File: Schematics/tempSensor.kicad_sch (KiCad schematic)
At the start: 0 parts

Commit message: Temp Sensors Circuitry
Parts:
- added A? (x4): ZTP-148SRC1, XDCR_ZTP-148SRC1, symbol SFRLibraries:ZTP-148SRC1
- added D?: D_Schottky, symbol Device:D_Schottky
- added R? (x4): 100k, symbol Device:R_Small_US
- added R? (x8): 1k, symbol Device:R_Small_US
- added R?: 10k, symbol Device:R_Small_US
- added U? (x2): AD8539ARMZ-REEL, RM_8_ADI, symbol SFRLibraries:AD8539ARMZ-REEL
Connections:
- new net: A?.2 (THERMOPILE), U?.3 (INA+) (x2)
- new net: R?.1, U?.2 (INA-) (x2)
- new net: A?.2 (THERMOPILE), U?.5 (INB+) (x2)
- new net: R?.1, U?.6 (INB-) (x2)
- new net Earth: A?.1 (THERMISTOR_GND), A?.1 (THERMISTOR_GND), A?.1 (THERMISTOR_GND), A?.1 (THERMISTOR_GND), D?.2 (A), U?.4 (V-), U?.4 (V-)
- new net Shifted Ground: A?.4 (THERMOPILE_GND), A?.4 (THERMOPILE_GND), A?.4 (THERMOPILE_GND), A?.4 (THERMOPILE_GND), D?.1 (K), R?.2, R?.2, R?.2, R?.2, R?.2
- new net ThermistorA: A?.3 (THERMISTOR), R?.2
- new net ThermistorB: A?.3 (THERMISTOR), R?.2
- new net ThermistorC: A?.3 (THERMISTOR), R?.2
- new net ThermistorD: A?.3 (THERMISTOR), R?.2
- new net ThermopileA: R?.1, R?.2, U?.7 (OUTB)
- new net ThermopileB: R?.1, R?.2, U?.1 (OUTA)
- new net ThermopileC: R?.1, R?.2, U?.7 (OUTB)
- new net ThermopileD: R?.1, R?.2, U?.1 (OUTA)
- new net VCC: R?.1, R?.1, R?.1, R?.1, R?.1, U?.8 (V+), U?.8 (V+)
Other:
- note added: "Create virtual ground for op amps so if thermopile goes negative relative to ground it will still be amplified as a positive voltage"
- note added: "Non-Inverting Op Amp"
- note added: "Voltage Divider for Thermistor"

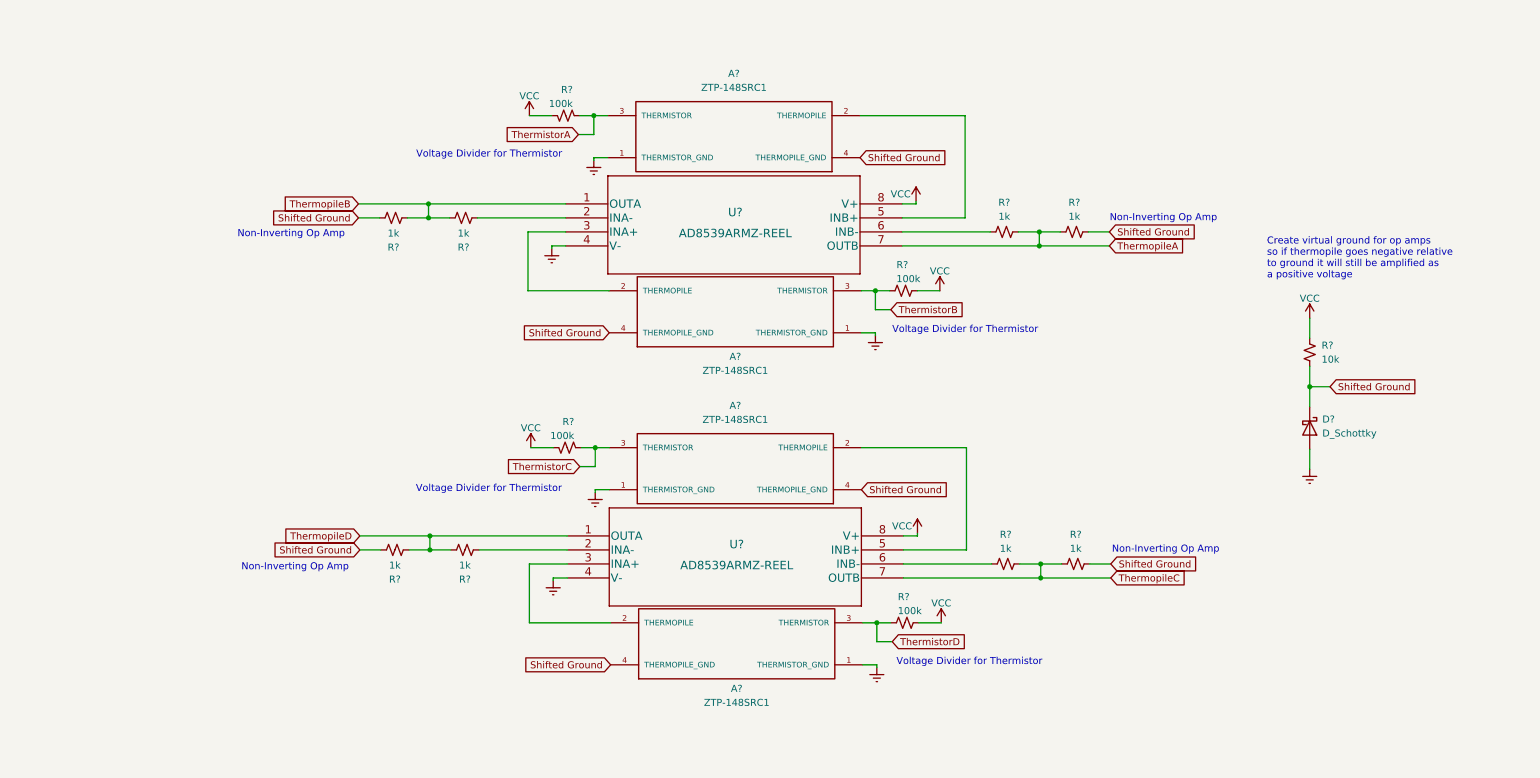
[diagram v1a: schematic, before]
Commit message: Changed MCU
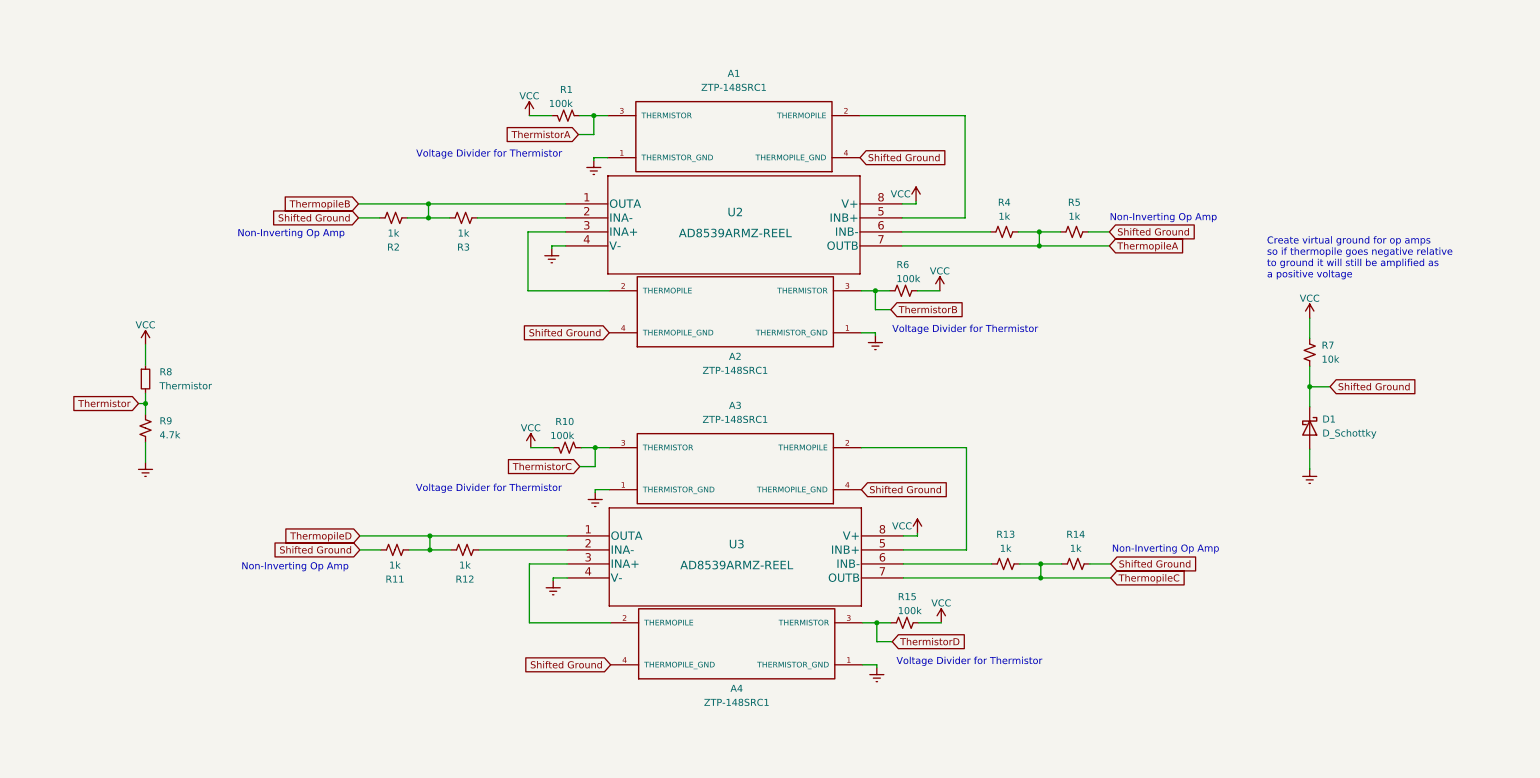
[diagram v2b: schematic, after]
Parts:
- added R8: Thermistor, symbol Device:R_Small
- added R9: 4.7k, symbol Device:R_Small_US
- gave numbers to parts that had none: 20
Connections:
- net Earth: now also R9.2
- net VCC: now also R8.1
- new net Thermistor: R8.2, R9.1

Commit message: Added Footprints
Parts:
- A1, A2, A3, A4: footprint XDCR_ZTP-148SRC1 -> SFRFootprints:Thermopile
- D1: footprint (none) -> Diode_SMD:D_SOD-323
- R1, R10, R11, R12, R13, R14, R15, R2, R3, R4, R5, R6, R7, R9: footprint (none) -> Resistor_SMD:R_0603_1608Metric_Pad0.98x0.95mm_HandSolder
- R8: footprint (none) -> Resistor_SMD:R_1206_3216Metric_Pad1.30x1.75mm_HandSolder
- U2, U3: footprint RM_8_ADI -> SFRFootprints:AD8539ARMZ-REEL
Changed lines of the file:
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@@
       (effects (font (size 1.27 1.27)) (justify left))
     )
-    (property "Footprint" "" (id 2) (at 40.64 107.95 0)
+    (property "Footprint" "Resistor_SMD:R_0603_1608Metric_Pad0.98x0.95mm_HandSolder" (id 2) (at 40.64 107.95 0)
       (effects (font (size 1.27 1.27)) hide)
     )
@@
     (property "Reference" "A4" (id 0) (at 147.828 155.194 0))
     (property "Value" "ZTP-148SRC1" (id 1) (at 147.828 157.734 0))
-    (property "Footprint" "XDCR_ZTP-148SRC1" (id 2) (at 137.668 131.191 0)
+    (property "Footprint" "SFRFootprints:Thermopile" (id 2) (at 137.668 131.191 0)
       (effects (font (size 1.27 1.27)) (justify left bottom) hide)
     )
@@
       (effects (font (size 1.27 1.27)) (justify left))
     )
-    (property "Footprint" "" (id 2) (at 116.84 51.308 0)
+    (property "Footprint" "Resistor_SMD:R_0603_1608Metric_Pad0.98x0.95mm_HandSolder" (id 2) (at 116.84 51.308 0)
       (effects (font (size 1.27 1.27)) hide)
     )
@@
       (effects (font (size 1.524 1.524)))
     )
-    (property "Footprint" "RM_8_ADI" (id 2) (at 147.32 61.214 0)
+    (property "Footprint" "SFRFootprints:AD8539ARMZ-REEL" (id 2) (at 147.32 61.214 0)
       (effects (font (size 1.524 1.524)) hide)
     )
@@
       (effects (font (size 1.27 1.27)) (justify left))
     )
-    (property "Footprint" "" (id 2) (at 117.094 111.506 0)
+    (property "Footprint" "Resistor_SMD:R_0603_1608Metric_Pad0.98x0.95mm_HandSolder" (id 2) (at 117.094 111.506 0)
       (effects (font (size 1.27 1.27)) hide)
     )
@@
     (property "Reference" "R2" (id 0) (at 85.598 75.184 90))
     (property "Value" "1k" (id 1) (at 85.598 72.644 90))
-    (property "Footprint" "" (id 2) (at 85.598 69.85 0)
+    (property "Footprint" "Resistor_SMD:R_0603_1608Metric_Pad0.98x0.95mm_HandSolder" (id 2) (at 85.598 69.85 0)
       (effects (font (size 1.27 1.27)) hide)
     )
@@
     (property "Reference" "R13" (id 0) (at 196.596 127.254 90))
     (property "Value" "1k" (id 1) (at 196.596 129.794 90))
-    (property "Footprint" "" (id 2) (at 196.596 132.588 0)
+    (property "Footprint" "Resistor_SMD:R_0603_1608Metric_Pad0.98x0.95mm_HandSolder" (id 2) (at 196.596 132.588 0)
       (effects (font (size 1.27 1.27)) hide)
     )
@@
       (effects (font (size 1.524 1.524)))
     )
-    (property "Footprint" "RM_8_ADI" (id 2) (at 147.574 121.412 0)
+    (property "Footprint" "SFRFootprints:AD8539ARMZ-REEL" (id 2) (at 147.574 121.412 0)
       (effects (font (size 1.524 1.524)) hide)
     )
@@
     (property "Reference" "R4" (id 0) (at 196.342 67.056 90))
     (property "Value" "1k" (id 1) (at 196.342 69.596 90))
-    (property "Footprint" "" (id 2) (at 196.342 72.39 0)
+    (property "Footprint" "Resistor_SMD:R_0603_1608Metric_Pad0.98x0.95mm_HandSolder" (id 2) (at 196.342 72.39 0)
       (effects (font (size 1.27 1.27)) hide)
     )
@@
     (property "Reference" "R5" (id 0) (at 209.042 67.056 90))
     (property "Value" "1k" (id 1) (at 209.042 69.596 90))
-    (property "Footprint" "" (id 2) (at 209.042 72.39 0)
+    (property "Footprint" "Resistor_SMD:R_0603_1608Metric_Pad0.98x0.95mm_HandSolder" (id 2) (at 209.042 72.39 0)
       (effects (font (size 1.27 1.27)) hide)
     )
@@
     (property "Reference" "R11" (id 0) (at 85.852 135.382 90))
     (property "Value" "1k" (id 1) (at 85.852 132.842 90))
-    (property "Footprint" "" (id 2) (at 85.852 130.048 0)
+    (property "Footprint" "Resistor_SMD:R_0603_1608Metric_Pad0.98x0.95mm_HandSolder" (id 2) (at 85.852 130.048 0)
       (effects (font (size 1.27 1.27)) hide)
     )
@@
       (effects (font (size 1.27 1.27)) (justify left))
     )
-    (property "Footprint" "" (id 2) (at 251.714 94.234 0)
+    (property "Footprint" "Resistor_SMD:R_0603_1608Metric_Pad0.98x0.95mm_HandSolder" (id 2) (at 251.714 94.234 0)
       (effects (font (size 1.27 1.27)) hide)
     )
@@
       (effects (font (size 1.27 1.27)) (justify left))
     )
-    (property "Footprint" "" (id 2) (at 178.308 143.256 0)
+    (property "Footprint" "Resistor_SMD:R_0603_1608Metric_Pad0.98x0.95mm_HandSolder" (id 2) (at 178.308 143.256 0)
       (effects (font (size 1.27 1.27)) hide)
     )
@@
     (property "Reference" "A3" (id 0) (at 147.574 103.886 0))
     (property "Value" "ZTP-148SRC1" (id 1) (at 147.574 106.426 0))
-    (property "Footprint" "XDCR_ZTP-148SRC1" (id 2) (at 157.734 99.441 0)
+    (property "Footprint" "SFRFootprints:Thermopile" (id 2) (at 157.734 99.441 0)
       (effects (font (size 1.27 1.27)) (justify left bottom) hide)
     )
@@
       (effects (font (size 1.27 1.27)) (justify left))
     )
-    (property "Footprint" "" (id 2) (at 40.64 99.06 0)
+    (property "Footprint" "Resistor_SMD:R_1206_3216Metric_Pad1.30x1.75mm_HandSolder" (id 2) (at 40.64 99.06 0)
       (effects (font (size 1.27 1.27)) hide)
     )
@@
     (property "Reference" "R12" (id 0) (at 98.552 135.382 90))
     (property "Value" "1k" (id 1) (at 98.552 132.842 90))
-    (property "Footprint" "" (id 2) (at 98.552 130.048 0)
+    (property "Footprint" "Resistor_SMD:R_0603_1608Metric_Pad0.98x0.95mm_HandSolder" (id 2) (at 98.552 130.048 0)
       (effects (font (size 1.27 1.27)) hide)
     )
@@
     (property "Reference" "R14" (id 0) (at 209.296 127.254 90))
     (property "Value" "1k" (id 1) (at 209.296 129.794 90))
-    (property "Footprint" "" (id 2) (at 209.296 132.588 0)
+    (property "Footprint" "Resistor_SMD:R_0603_1608Metric_Pad0.98x0.95mm_HandSolder" (id 2) (at 209.296 132.588 0)
       (effects (font (size 1.27 1.27)) hide)
     )
@@
     (property "Reference" "A1" (id 0) (at 147.32 43.688 0))
     (property "Value" "ZTP-148SRC1" (id 1) (at 147.32 46.228 0))
-    (property "Footprint" "XDCR_ZTP-148SRC1" (id 2) (at 157.48 39.243 0)
+    (property "Footprint" "SFRFootprints:Thermopile" (id 2) (at 157.48 39.243 0)
       (effects (font (size 1.27 1.27)) (justify left bottom) hide)
     )
@@
     (property "Reference" "R3" (id 0) (at 98.298 75.184 90))
     (property "Value" "1k" (id 1) (at 98.298 72.644 90))
-    (property "Footprint" "" (id 2) (at 98.298 69.85 0)
+    (property "Footprint" "Resistor_SMD:R_0603_1608Metric_Pad0.98x0.95mm_HandSolder" (id 2) (at 98.298 69.85 0)
       (effects (font (size 1.27 1.27)) hide)
     )
@@
     (property "Reference" "A2" (id 0) (at 147.574 94.996 0))
     (property "Value" "ZTP-148SRC1" (id 1) (at 147.574 97.536 0))
-    (property "Footprint" "XDCR_ZTP-148SRC1" (id 2) (at 137.414 70.993 0)
+    (property "Footprint" "SFRFootprints:Thermopile" (id 2) (at 137.414 70.993 0)
       (effects (font (size 1.27 1.27)) (justify left bottom) hide)
     )
@@
       (effects (font (size 1.27 1.27)) (justify left))
     )
-    (property "Footprint" "" (id 2) (at 178.054 83.058 0)
+    (property "Footprint" "Resistor_SMD:R_0603_1608Metric_Pad0.98x0.95mm_HandSolder" (id 2) (at 178.054 83.058 0)
       (effects (font (size 1.27 1.27)) hide)
     )
@@
       (effects (font (size 1.27 1.27)) (justify left))
     )
-    (property "Footprint" "" (id 2) (at 251.714 107.95 0)
-      (effects (font (size 1.27 1.27)) hide)
-    )
+    (property "Footprint" "Diode_SMD:D_SOD-323" (id 2) (at 251.714 107.95 0)
+      (effects (font (size 1.27 1.27)) hide)
+    )

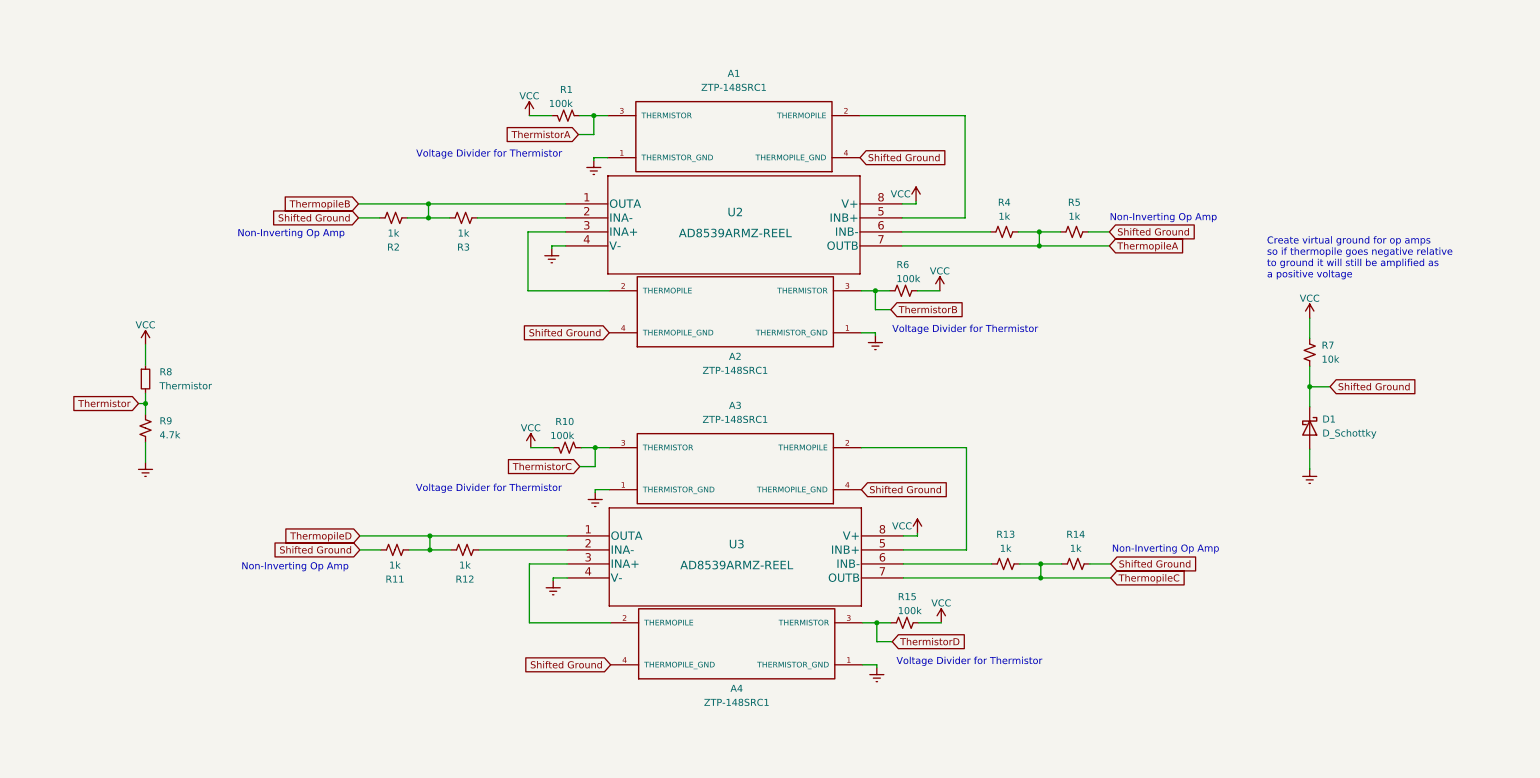
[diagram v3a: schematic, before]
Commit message: Fixed IR Sensor
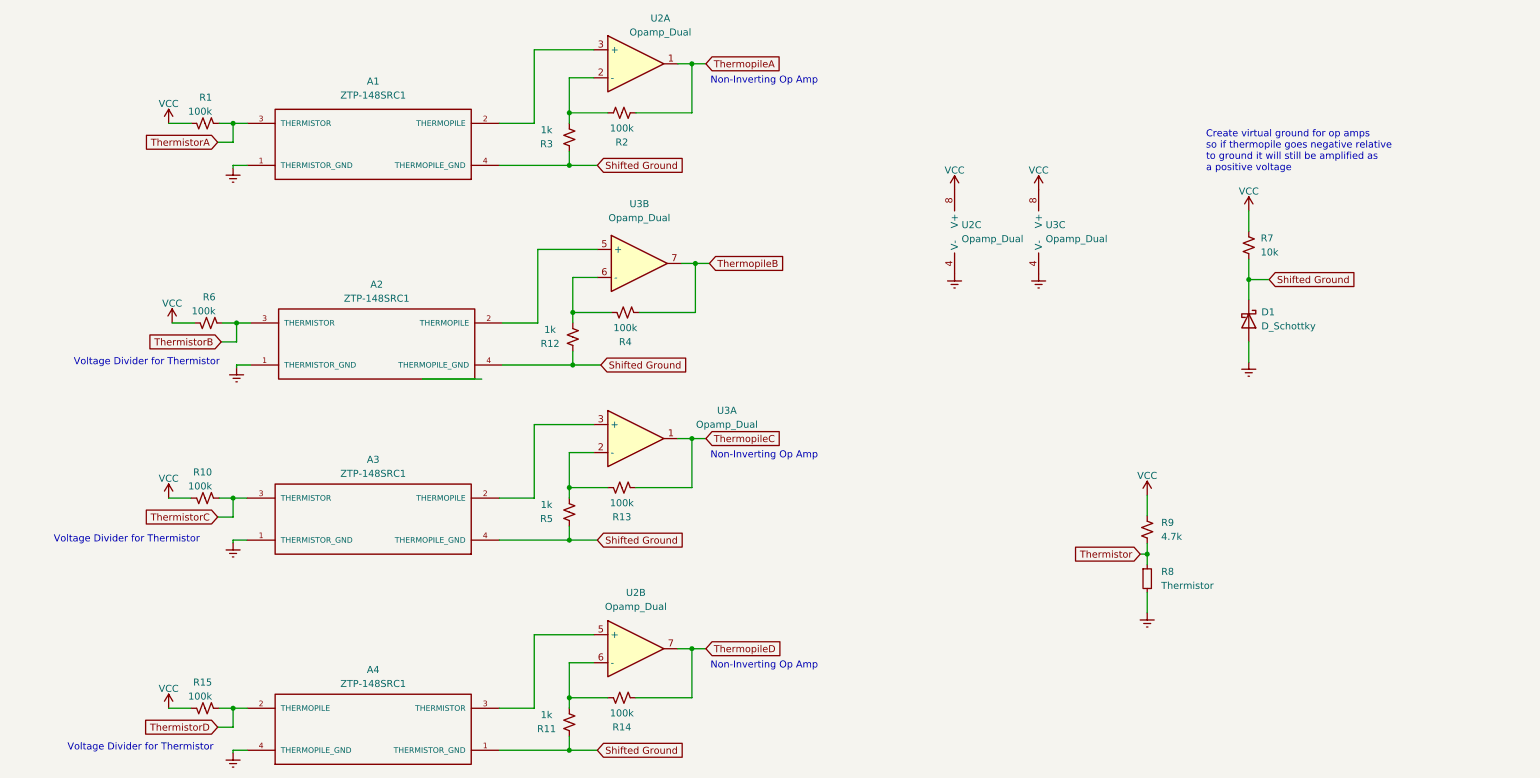
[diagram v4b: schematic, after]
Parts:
- removed U2, U3: AD8539ARMZ-REEL, SFRFootprints:AD8539ARMZ-REEL, symbol SFRLibraries:AD8539ARMZ-REEL
- added U2, U3: Opamp_Dual, SFRFootprints:AD8539ARMZ-REEL, symbol Device:Opamp_Dual
- R13, R14, R2, R4: value 1k -> 100k
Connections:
- net Earth: now also A4.4 (THERMOPILE_GND), R8.2, U2.4 (V-), U3.4 (V-); no longer A4.1 (THERMISTOR_GND), R9.2
- net Shifted Ground: now also A4.1 (THERMISTOR_GND), R11.1, R12.1, R3.1, R5.1; no longer A4.4 (THERMOPILE_GND), R11.2, R14.2, R2.2, R5.2
- net Thermistor: now also R8.1, R9.2; no longer R8.2, R9.1
- net ThermistorD: now also A4.2 (THERMOPILE); no longer A4.3 (THERMISTOR)
- net ThermopileA: now also R2.1, U2.1; no longer R4.2, R5.1
- net ThermopileB: now also R4.2, U3.7; no longer R2.1, R3.2
- net ThermopileC: now also U3.1; no longer R14.1
- net ThermopileD: now also R14.2, U2.7; no longer R11.1, R12.2
- net VCC: now also R9.1, U2.8 (V+), U3.8 (V+); no longer R8.1
- net at A2.2 (THERMOPILE): now also U3.5 (+)
- net at A1.2 (THERMOPILE): now also U2.3 (+)
- net at R4.1: now also R12.2, U3.6 (-)
- net at R13.1: now also R5.2, U3.2 (-)
- net at A3.2 (THERMOPILE): now also U3.3 (+)
- new net: A4.3 (THERMISTOR), U2.5 (+)
- new net: R11.2, R14.1, U2.6 (-)
- new net: R2.2, R3.2, U2.2 (-)
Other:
- moved on the sheet: A1, A2, A3, A4, D1, R1, R10, R11, R12, R13, R14, R15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

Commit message: Finalized PCB
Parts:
- renumbered U3 to U2, U2 to U3
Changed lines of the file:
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@@
   (symbol (lib_id "Device:Opamp_Dual") (at 129.54 109.855 0) (unit 1)
     (in_bom yes) (on_board yes)
-    (property "Reference" "U3" (id 0) (at 146.05 104.775 0))
-    (property "Value" "Opamp_Dual" (id 1) (at 146.05 107.315 0))
+    (property "Reference" "U3" (id 0) (at 135.255 103.505 0))
+    (property "Value" "Opamp_Dual" (id 1) (at 135.255 106.045 0))
     (property "Footprint" "SFRFootprints:AD8539ARMZ-REEL" (id 2) (at 129.54 109.855 0)
       (effects (font (size 1.27 1.27)) hide)
@@
   )
   (symbol (lib_id "Device:Opamp_Dual") (at 129.54 147.955 0) (unit 2)
-    (in_bom yes) (on_board yes) (fields_autoplaced)
-    (property "Reference" "U2" (id 0) (at 129.54 137.795 0))
-    (property "Value" "Opamp_Dual" (id 1) (at 129.54 140.335 0))
+    (in_bom yes) (on_board yes)
+    (property "Reference" "U3" (id 0) (at 133.985 140.335 0))
+    (property "Value" "Opamp_Dual" (id 1) (at 133.985 142.875 0))
     (property "Footprint" "SFRFootprints:AD8539ARMZ-REEL" (id 2) (at 129.54 147.955 0)
       (effects (font (size 1.27 1.27)) hide)
@@
   )
   (symbol (lib_id "Device:Opamp_Dual") (at 130.175 78.105 0) (unit 2)
-    (in_bom yes) (on_board yes) (fields_autoplaced)
-    (property "Reference" "U3" (id 0) (at 130.175 67.31 0))
-    (property "Value" "Opamp_Dual" (id 1) (at 130.175 69.85 0))
+    (in_bom yes) (on_board yes)
+    (property "Reference" "U2" (id 0) (at 134.62 71.12 0))
+    (property "Value" "Opamp_Dual" (id 1) (at 134.62 73.66 0))
     (property "Footprint" "SFRFootprints:AD8539ARMZ-REEL" (id 2) (at 130.175 78.105 0)
       (effects (font (size 1.27 1.27)) hide)
